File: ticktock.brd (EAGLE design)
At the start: 61 x 67.3 mm, 64 parts, among them IC1 ATMEGA644A, IC2 AD8611RM, IC3 REF200U, J1 AVR_SPI_PRG_6NS, Q1 MOSFET-NCHANNEL2N7002PW, Q2 MOSFET-NCHANNELBSS138, Q3 MOSFET-NCHANNELBSS138, U1 MAX232SOIC16, U2 OSCILLATORSMD, U3 FT232RLSSOP, U4 BMP180, X1 RS232

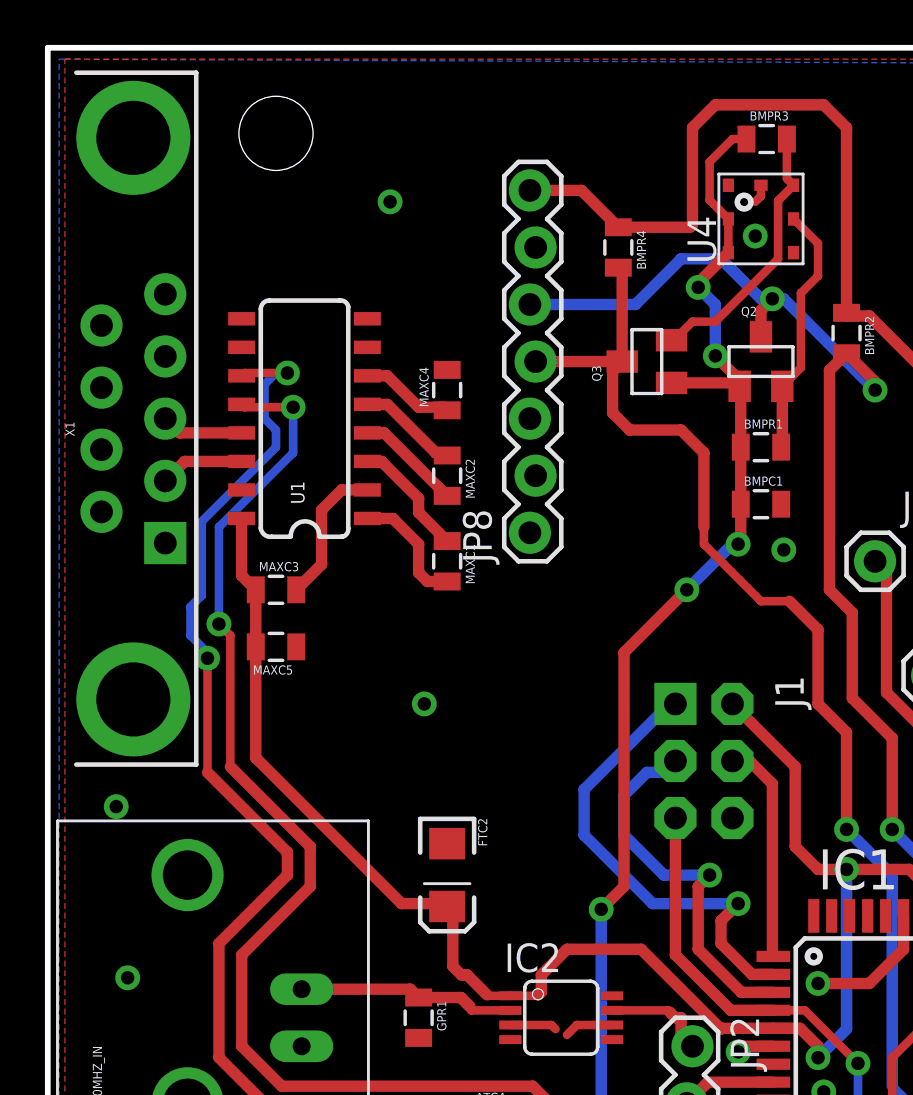
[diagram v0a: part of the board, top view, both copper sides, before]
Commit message: Remove BMP carrier board header and Pull RS232 connector back to PCB edge
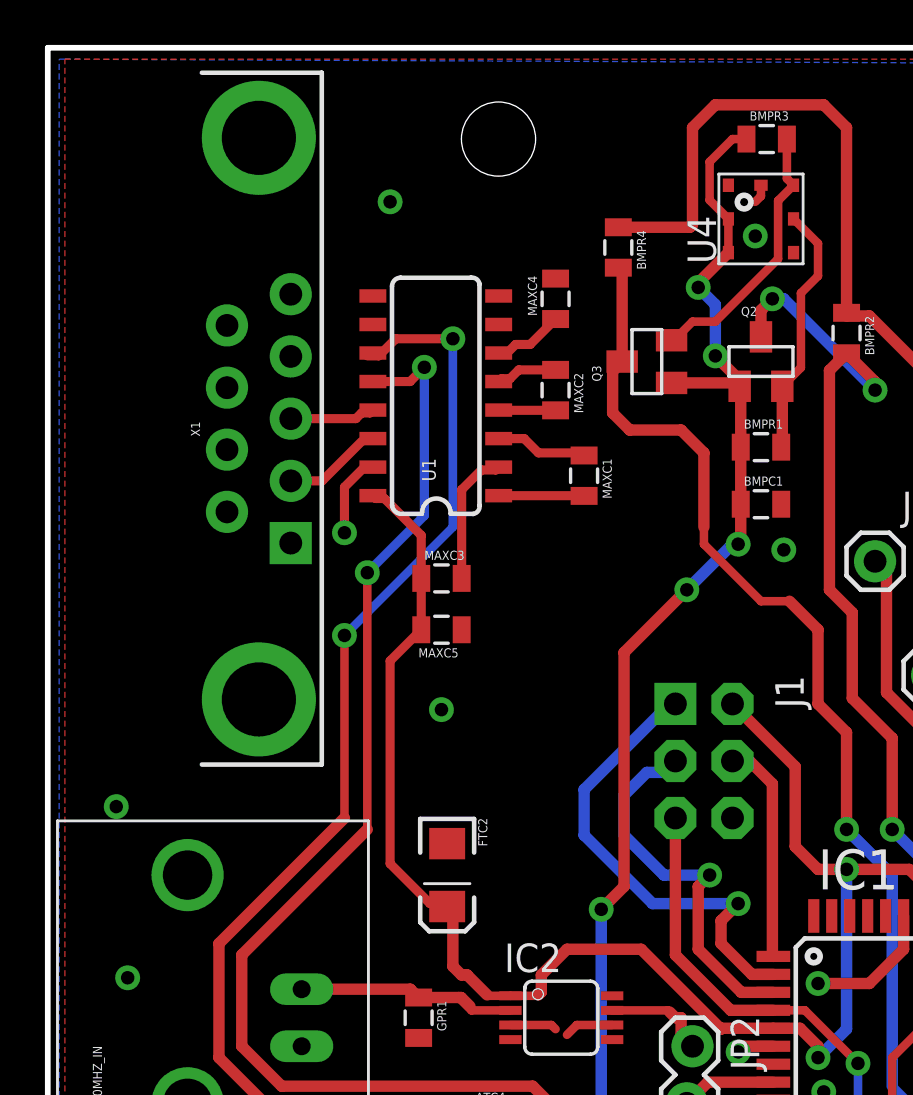
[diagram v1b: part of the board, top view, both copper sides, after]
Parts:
- removed JP8: 7-Pin, SparkFun-Connectors:1X07_LOCK
- moved STANDOFF2 9.91 mm to (20.1, 63.2)
- moved MAXC5 7.41 mm to (17.5, 41.4)
- moved MAXC3 7.38 mm to (17.5, 43.7)
- moved MAXC1 7.19 mm to (23.9, 48.3)
- moved MAXC4 6.31 mm to (22.6, 56.1)
- moved MAXC2 6.15 mm to (22.6, 52.1)
- moved U1 5.93 mm to (17.3, 51.8)
- moved X1 5.59 mm to (9.40, 50.8)
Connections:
- net 5V: no longer JP8.7
- net GND: no longer JP8.1
- net I2C_SCL: no longer JP8.5
- net I2C_SDA: no longer JP8.4
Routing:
- net I2C_SCL: track 61.7 -> 49.3 mm
- net 5V: track 300.3 -> 294.8 mm
- net I2C_SDA: track 54.9 -> 51.0 mm
- net GND: track 41.0 -> 44.6 mm, vias 29 -> 30
- net GPS_TX: track 99.2 -> 101.5 mm
- net N$5: track 4.71 -> 2.54 mm
- net N$6: track 4.49 -> 2.75 mm
- net N$3: track 5.46 -> 3.81 mm
- net N$4: track 5.38 -> 4.12 mm
- net GPS_RX: track 66.1 -> 67.1 mm
- net N$9: track 4.19 -> 3.16 mm

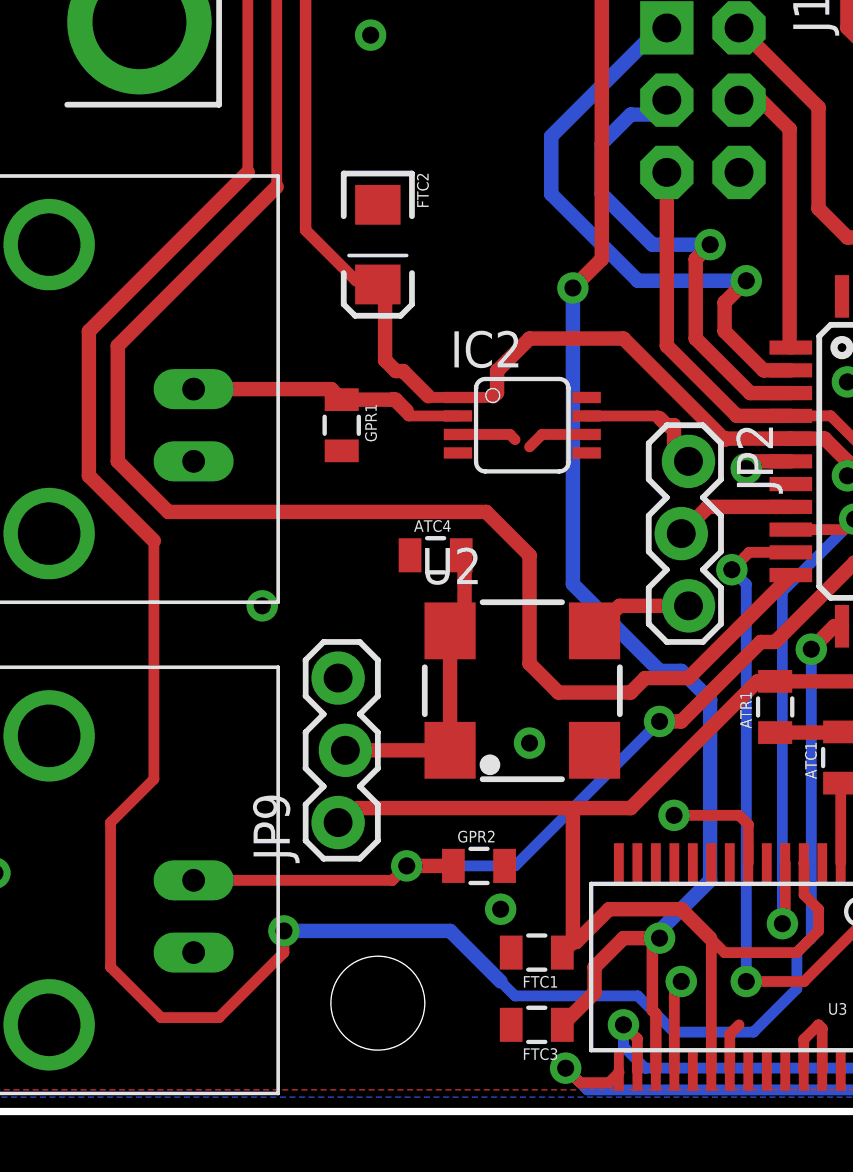
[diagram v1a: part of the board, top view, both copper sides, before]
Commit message: Move 10uF cap closer to FTDI chip
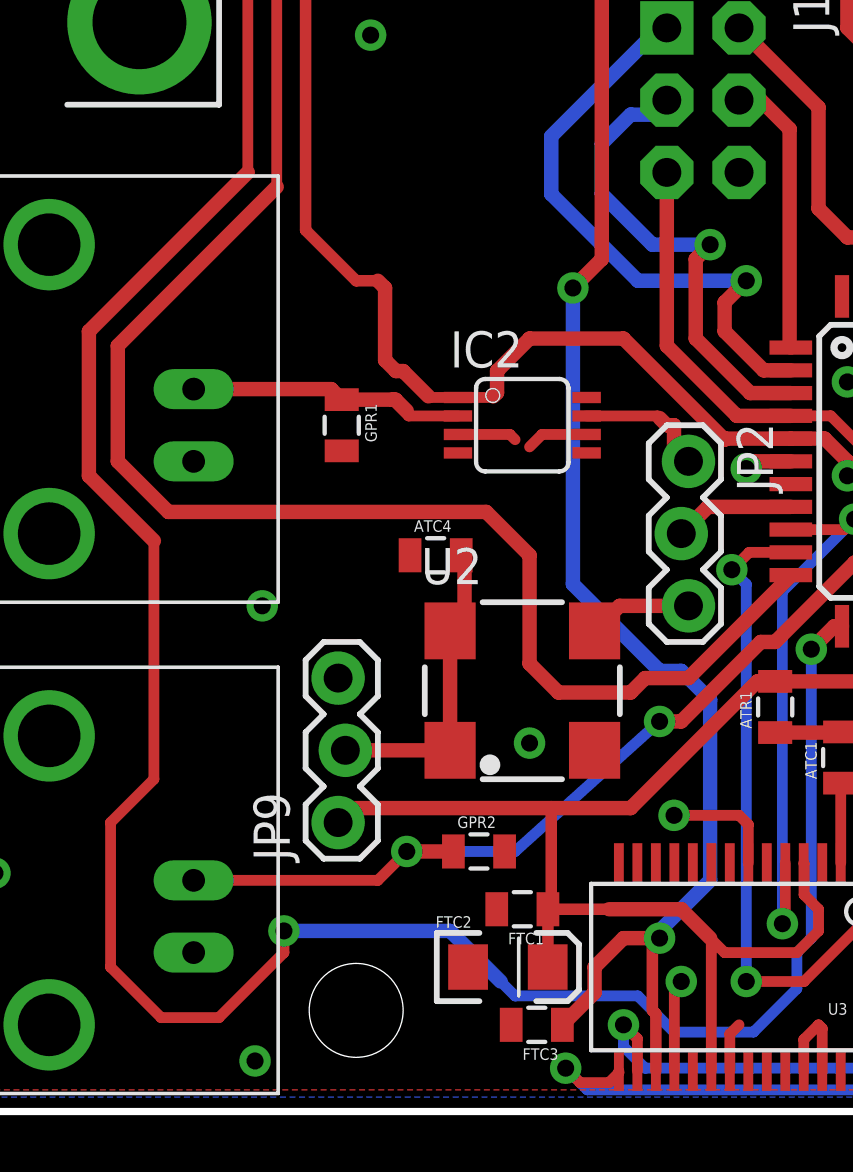
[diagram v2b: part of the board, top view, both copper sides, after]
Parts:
- moved FTC2 25.8 mm to (22.4, 5.08), turned to 0 degrees
- moved FTC1 1.61 mm to (22.9, 7.11)
- moved STANDOFF4 0.80 mm to (17.0, 3.56)
- moved GPR2 0.51 mm to (21.3, 9.14)
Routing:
- net 5V: track 294.8 -> 295.3 mm
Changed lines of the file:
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@@
 <attribute name="PROD_ID" value="CONN-08278" x="44.45" y="8.89" size="1.778" layer="27" rot="R90" display="off"/>
 </element>
-<element name="FTC1" library="SparkFun-Capacitors" package="0805" value="0.1uF" x="23.368" y="5.588" rot="R180"/>
+<element name="FTC1" library="SparkFun-Capacitors" package="0805" value="0.1uF" x="22.86" y="7.112" rot="R180"/>
 <element name="FTC3" library="SparkFun-Capacitors" package="0805" value="0.1uF" x="23.368" y="3.048" rot="R180"/>
 <element name="ATC1" library="SparkFun-Capacitors" package="0805" value="0.1uF" x="34.036" y="12.446" rot="R90"/>
-<element name="FTC2" library="SparkFun-Capacitors" package="EIA3216" value="10uF" x="17.78" y="30.48" rot="R270"/>
+<element name="FTC2" library="SparkFun-Capacitors" package="EIA3216" value="10uF" x="22.352" y="5.08"/>
 <element name="ATR1" library="SparkFun-Resistors" package="0805" value="10K" x="31.75" y="14.224" rot="R90"/>
 <element name="ATC2" library="SparkFun-Capacitors" package="0805" value="0.1uF" x="39.116" y="13.97" rot="R180"/>
@@
 </element>
 <element name="GPR1" library="SparkFun-Resistors" package="0805" value="50" x="16.51" y="24.13" rot="R270"/>
-<element name="GPR2" library="SparkFun-Resistors" package="0805" value="50" x="21.336" y="8.636"/>
+<element name="GPR2" library="SparkFun-Resistors" package="0805" value="50" x="21.336" y="9.144"/>
 <element name="RFB" library="SparkFun-Resistors" package="0805" value="1K" x="53.34" y="24.13" rot="R270"/>
 <element name="CFB" library="SparkFun-Capacitors" package="0805" value="??" x="50.8" y="24.13" rot="R90"/>
@@
 <element name="STANDOFF2" library="SparkFun-Electromechanical" package="STAND-OFF" value="STAND-OFF" x="20.066" y="63.246"/>
 <element name="STANDOFF3" library="SparkFun-Electromechanical" package="STAND-OFF" value="STAND-OFF" x="56.642" y="15.24"/>
-<element name="STANDOFF4" library="SparkFun-Electromechanical" package="STAND-OFF" value="STAND-OFF" x="17.78" y="3.81"/>
+<element name="STANDOFF4" library="SparkFun-Electromechanical" package="STAND-OFF" value="STAND-OFF" x="17.018" y="3.556"/>
 <element name="JP9" library="SparkFun-Connectors" package="1X03_LOCK" value="3-Pin" x="16.51" y="10.16" rot="R90"/>
 </elements>
@@
 <wire x1="52.72" y1="19.346" x2="52.07" y2="19.996" width="0.381" layer="1"/>
 <via x="23.114" y="12.954" extent="1-16" drill="0.6"/>
-<via x="22.098" y="7.112" extent="1-16" drill="0.6"/>
+<via x="13.462" y="1.778" extent="1-16" drill="0.6"/>
 <wire x1="33.405" y1="1.424" x2="33.405" y2="2.917" width="0.381" layer="1"/>
 <wire x1="33.405" y1="2.917" x2="33.274" y2="3.048" width="0.381" layer="1"/>
@@
 <wire x1="31.126" y1="15.124" x2="26.67" y2="10.668" width="0.508" layer="1"/>
 <wire x1="16.383" y1="10.16" x2="16.891" y2="10.668" width="0.508" layer="1"/>
-<wire x1="16.891" y1="10.668" x2="24.638" y2="10.668" width="0.508" layer="1"/>
-<wire x1="24.638" y1="10.668" x2="26.67" y2="10.668" width="0.508" layer="1"/>
-<wire x1="24.268" y1="5.588" x2="24.638" y2="5.958" width="0.508" layer="1"/>
-<wire x1="24.638" y1="5.958" x2="24.638" y2="10.668" width="0.508" layer="1"/>
+<wire x1="16.891" y1="10.668" x2="23.876" y2="10.668" width="0.508" layer="1"/>
+<wire x1="23.876" y1="10.668" x2="26.67" y2="10.668" width="0.508" layer="1"/>
 <wire x1="38.216" y1="13.97" x2="38.216" y2="13.6" width="0.508" layer="1"/>
 <wire x1="38.216" y1="13.6" x2="39.37" y2="12.446" width="0.508" layer="1"/>
@@
 <wire x1="52.46" y1="52.1" x2="39.908" y2="52.1" width="0.508" layer="1"/>
 <wire x1="39.908" y1="52.1" x2="39.878" y2="52.07" width="0.508" layer="1"/>
-<wire x1="17.78" y1="29.08" x2="17.78" y2="28.956" width="0.508" layer="1"/>
-<wire x1="17.78" y1="29.08" x2="17.78" y2="29.21" width="0.508" layer="1"/>
 <wire x1="17.78" y1="29.21" x2="18.034" y2="28.956" width="0.508" layer="1"/>
 <wire x1="18.034" y1="28.956" x2="18.034" y2="26.416" width="0.508" layer="1"/>
@@
 <wire x1="38.9" y1="28.66" x2="38.9" y2="27.216" width="0.508" layer="1"/>
 <wire x1="38.9" y1="27.216" x2="38.862" y2="27.178" width="0.508" layer="1"/>
-<wire x1="24.638" y1="5.958" x2="24.754" y2="5.958" width="0.508" layer="1"/>
-<wire x1="24.754" y1="5.958" x2="25.908" y2="7.112" width="0.508" layer="1"/>
 <wire x1="25.908" y1="7.112" x2="28.448" y2="7.112" width="0.508" layer="1"/>
 <wire x1="28.448" y1="7.112" x2="29.464" y2="6.096" width="0.508" layer="1"/>
@@
 <wire x1="15.24" y1="30.988" x2="15.24" y2="40.016" width="0.4064" layer="1"/>
 <wire x1="15.24" y1="40.016" x2="16.626" y2="41.402" width="0.4064" layer="1"/>
+<wire x1="23.76" y1="7.112" x2="23.76" y2="5.088" width="0.4064" layer="1"/>
+<wire x1="23.76" y1="5.088" x2="23.752" y2="5.08" width="0.4064" layer="1"/>
+<wire x1="23.76" y1="7.112" x2="23.876" y2="7.112" width="0.4064" layer="1"/>
+<wire x1="25.908" y1="7.112" x2="23.876" y2="7.112" width="0.4064" layer="1"/>
+<wire x1="23.876" y1="7.112" x2="23.876" y2="10.668" width="0.4064" layer="1"/>
 </signal>
 <signal name="N$1">
@@
 <contactref element="IC1" pad="15"/>
 <contactref element="GPR2" pad="1"/>
-<wire x1="18.796" y1="8.636" x2="20.436" y2="8.636" width="0.508" layer="1"/>
-<via x="18.796" y="8.636" extent="1-16" drill="0.6"/>
+<wire x1="18.796" y1="9.144" x2="20.436" y2="9.144" width="0.508" layer="1"/>
+<via x="18.796" y="9.144" extent="1-16" drill="0.6"/>
 <wire x1="36.5" y1="17.06" x2="36.5" y2="18.872" width="0.508" layer="1"/>
 <wire x1="36.5" y1="18.872" x2="36.068" y2="19.304" width="0.508" layer="1"/>
@@
 <wire x1="28.448" y1="13.716" x2="31.242" y2="16.51" width="0.508" layer="1"/>
 <wire x1="31.242" y1="16.51" x2="31.75" y2="16.51" width="0.508" layer="1"/>
-<wire x1="11.303" y1="8.128" x2="18.288" y2="8.128" width="0.381" layer="1"/>
-<wire x1="18.288" y1="8.128" x2="18.796" y2="8.636" width="0.381" layer="1"/>
-<wire x1="18.796" y1="8.636" x2="22.606" y2="8.636" width="0.381" layer="16"/>
-<wire x1="22.606" y1="8.636" x2="27.686" y2="13.716" width="0.381" layer="16"/>
+<wire x1="11.303" y1="8.128" x2="17.78" y2="8.128" width="0.381" layer="1"/>
+<wire x1="17.78" y1="8.128" x2="18.796" y2="9.144" width="0.381" layer="1"/>
+<wire x1="18.796" y1="9.144" x2="22.606" y2="9.144" width="0.381" layer="16"/>
+<wire x1="22.606" y1="9.144" x2="27.686" y2="13.716" width="0.381" layer="16"/>
 </signal>
 <signal name="GPS_10MHZ">
